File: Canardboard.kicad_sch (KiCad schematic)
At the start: 59 parts, among them J1 RBUS, J4 Conn_01x02_Male, J5 Conn_01x03_Male, J6 Conn_01x03_Male, J7 Conn_01x03_Male, Q1 SI4143DY-T1-GE3, Q2 SI4143DY-T1-GE3, U1 ESP32-S3, U10 LTC4412xS6, U9 LTC4412xS6, Y1 40MHz±10ppm

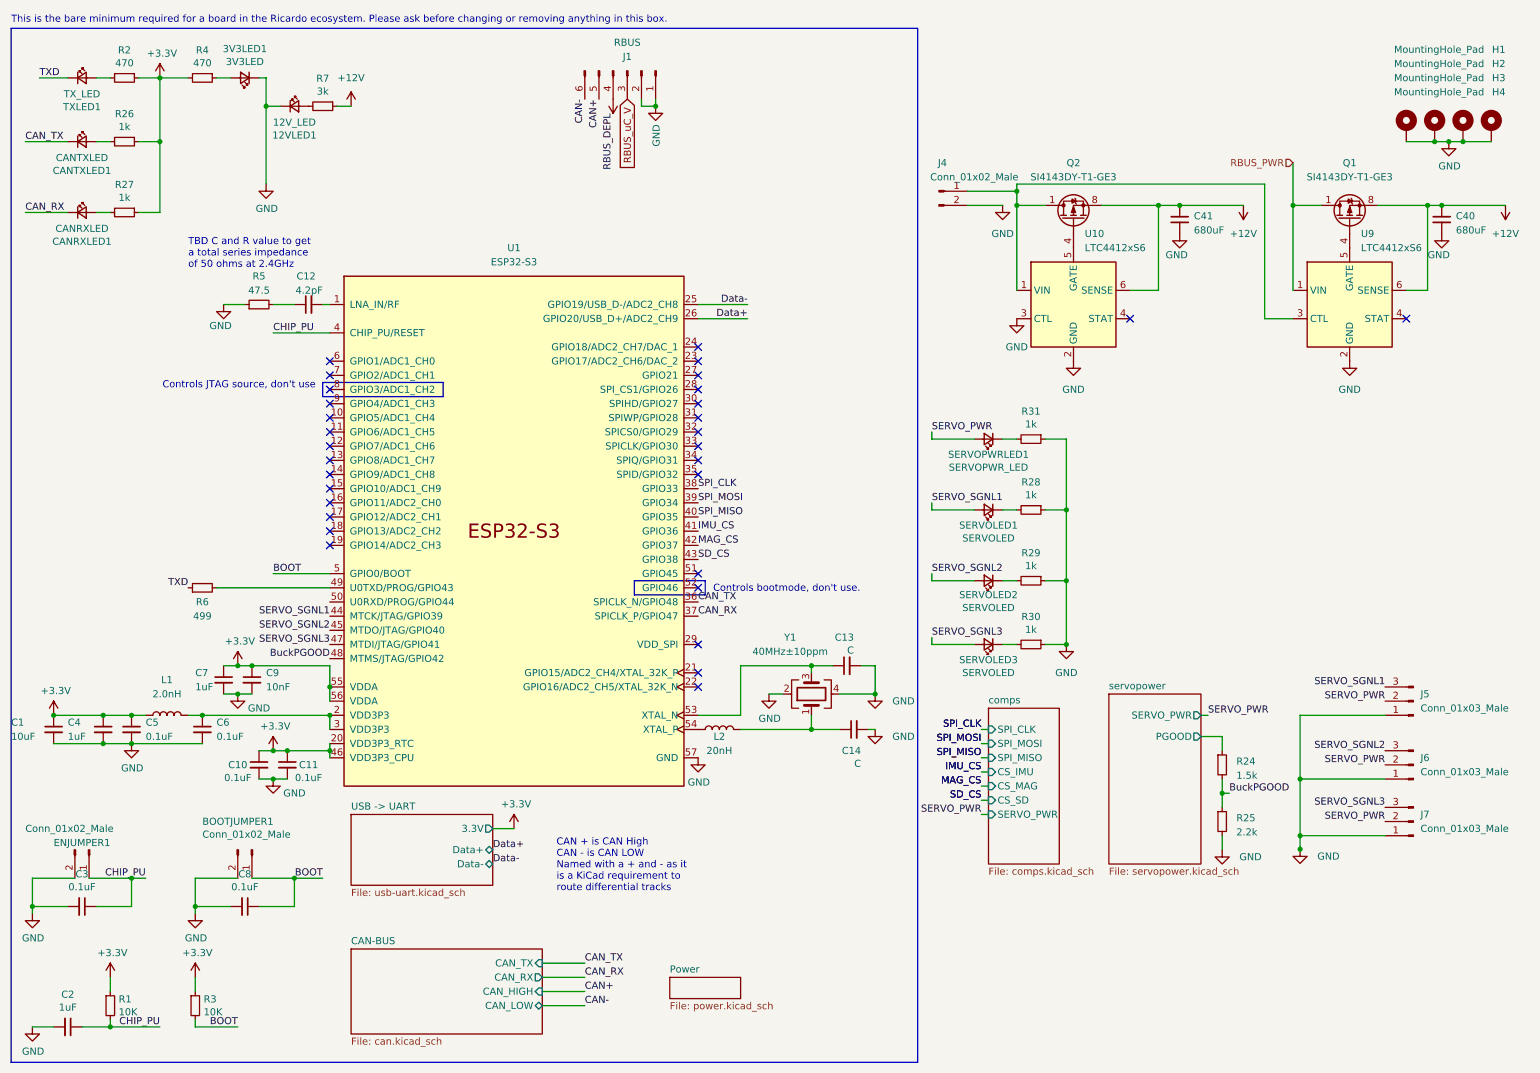
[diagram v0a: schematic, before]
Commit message: error encountered - battery logic and inductor
- use large capacitor?
- use VBUS as a power source?
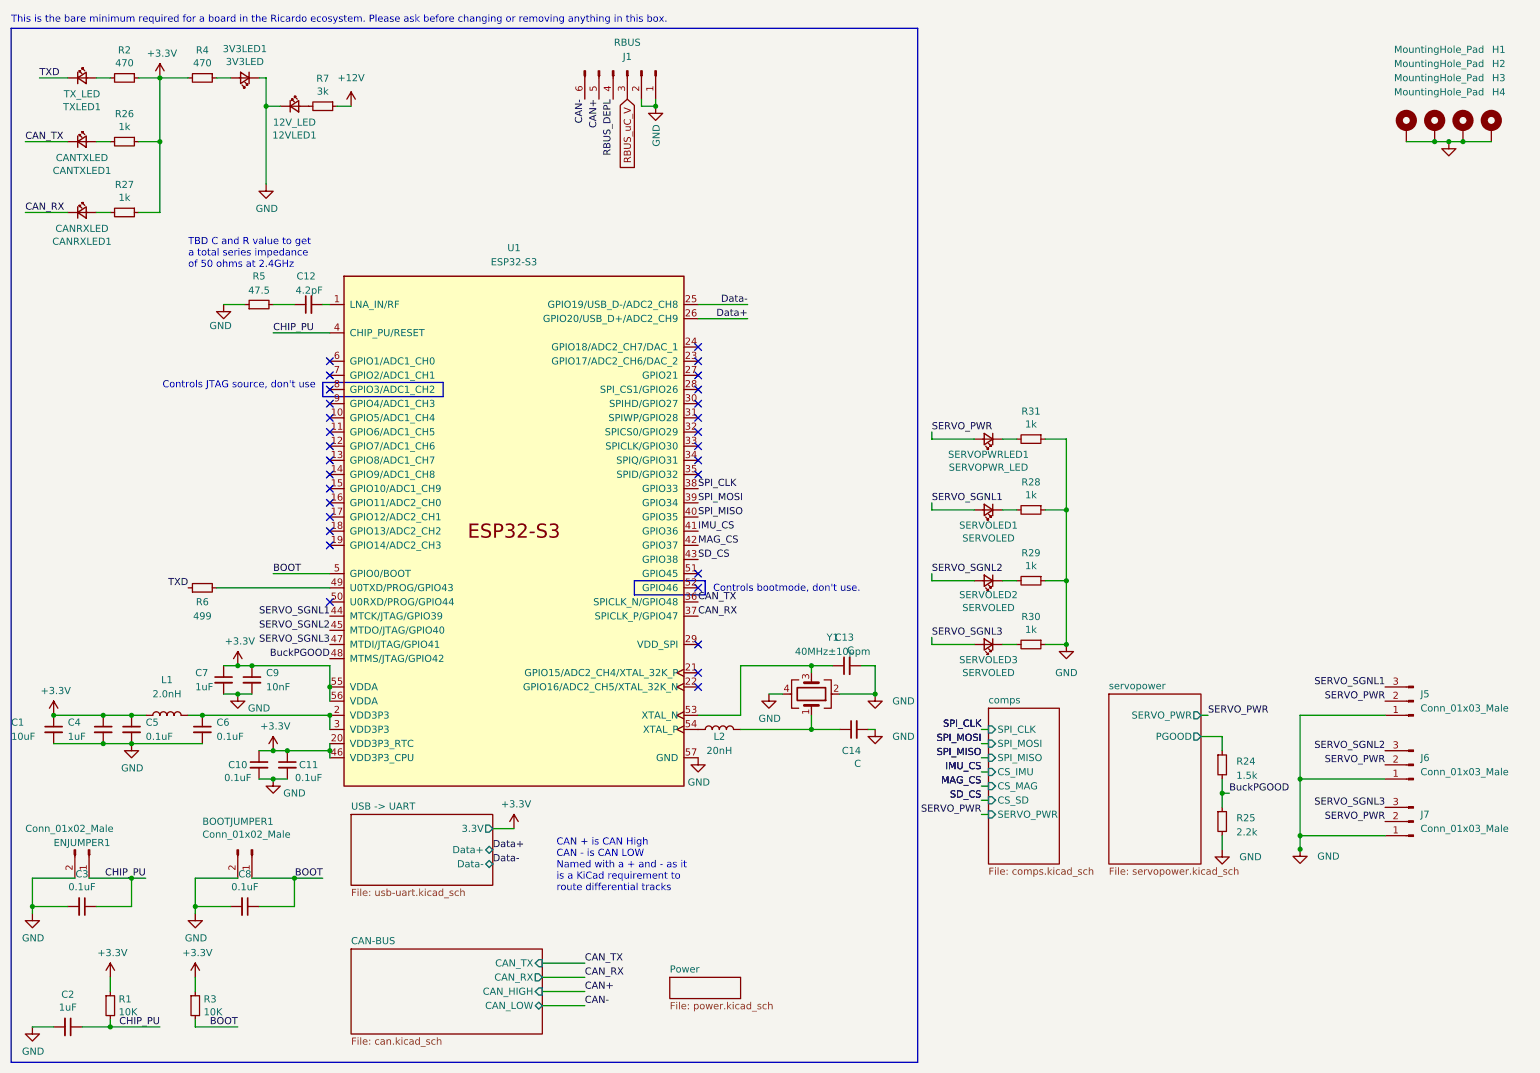
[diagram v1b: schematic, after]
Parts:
- removed C40, C41: 680uF, Capacitor_SMD:CP_Elec_10x10.5, symbol Device:C_Small
- removed J4: Conn_01x02_Male, iclr:AMASS_XT60PW-F, symbol Connector:Conn_01x02_Male
- removed Q1, Q2: SI4143DY-T1-GE3, Package_SO:SOIC-8_3.9x4.9mm_P1.27mm, symbol Device:Q_PMOS_GDS
- removed U10, U9: LTC4412xS6, Package_TO_SOT_SMD:TSOT-23-6, symbol Power_Management:LTC4412xS6
- J1: footprint Connector_Molex:Molex_Mini-Fit_Jr_5566-06A_2x03_P4.20mm_Vertical -> Connector_Molex:Molex_Mini-Fit_Jr_5569-06A2_2x03_P4.20mm_Horizontal
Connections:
- net +12V: no longer J1.4 (Pin_4)
- net RBUS_DEPL: now also J1.4 (Pin_4)
- no-connect marks 31 -> 30
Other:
- moved on the sheet: Y1

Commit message: power draft 2, power fixed I think
10 mosfets now!

2 each on:

Servo power: 3s/4s LIPO, RBUS_DEPL
3.3: VBUS, RBUS_3.3, 3s/4s LIPO

fixed some capacitors
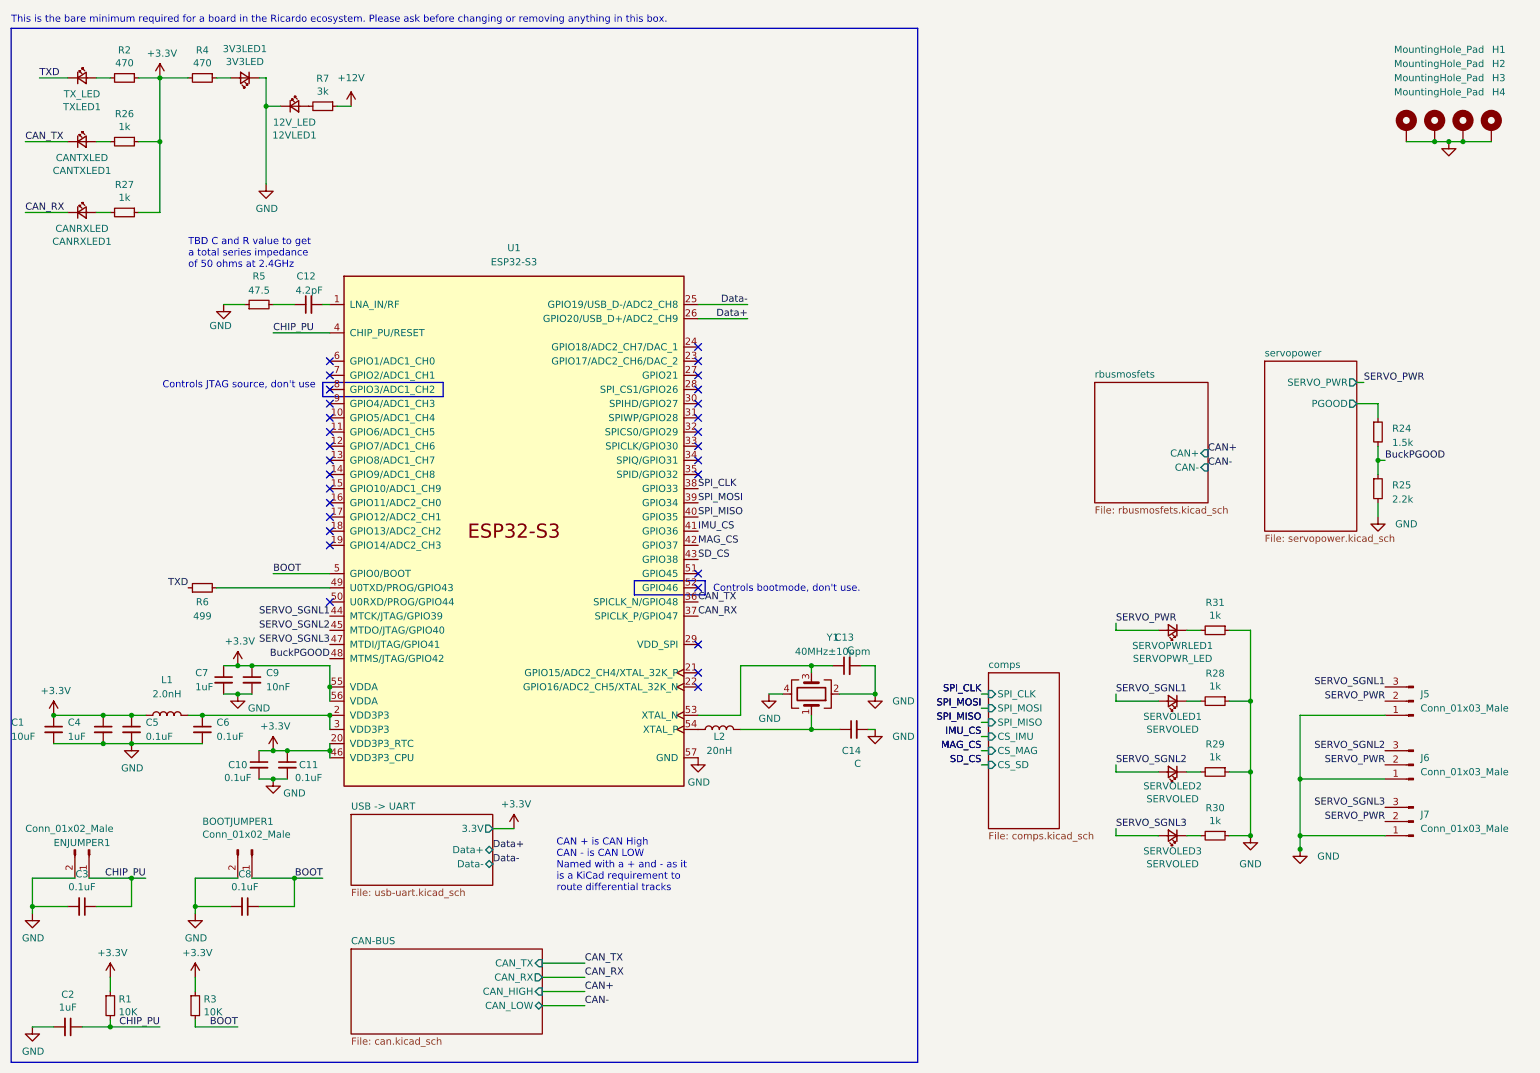
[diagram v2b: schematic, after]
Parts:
- removed J1: RBUS, Connector_Molex:Molex_Mini-Fit_Jr_5569-06A2_2x03_P4.20mm_Horizontal, symbol Connector:Conn_01x06_Male
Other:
- removed sheet Power
- added sheet rbusmosfets (rbusmosfets.kicad_sch)
- sheet comps ports: added none; removed SERVO_PWR
- moved on the sheet: R24, R25, R28, R29, R30, R31, SERVOLED1, SERVOLED2, SERVOLED3, SERVOPWRLED1

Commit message: PCB layout work
pcb layout work
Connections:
- net BOOT: now also BOOTJUMPER1.2 (Pin_2); no longer BOOTJUMPER1.1 (Pin_1)
- net GND: no longer BOOTJUMPER1.2 (Pin_2)
- net IMU_CS: now also U1.45 (MTDO/JTAG/GPIO40); no longer U1.41 (GPIO36)
- net MAG_CS: now also U1.47 (MTDI/JTAG/GPIO41); no longer U1.42 (GPIO37)
- net SD_CS: now also U1.38 (GPIO33); no longer U1.43 (GPIO38)
- net SERVO_SGNL1: now also U1.43 (GPIO38); no longer U1.44 (MTCK/JTAG/GPIO39)
- net SERVO_SGNL2: now also U1.42 (GPIO37); no longer U1.45 (MTDO/JTAG/GPIO40)
- net SERVO_SGNL3: now also U1.44 (MTCK/JTAG/GPIO39); no longer U1.47 (MTDI/JTAG/GPIO41)
- net SPI_CLK: now also U1.39 (GPIO34); no longer U1.38 (GPIO33)
- net SPI_MISO: now also U1.41 (GPIO36); no longer U1.40 (GPIO35)
- net SPI_MOSI: now also U1.40 (GPIO35); no longer U1.39 (GPIO34)
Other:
- moved on the sheet: BOOTJUMPER1
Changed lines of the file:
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@@
-    (stroke (width 0) (type default))
-  )
-  (wire (pts (xy 55.88 165.1) (xy 63.5 165.1))
     (stroke (width 0) (type default))
   )
@@
   )
   (wire (pts (xy 35.56 45.72) (xy 39.37 45.72))
+    (stroke (width 0) (type default))
+  )
+  (wire (pts (xy 58.42 165.1) (xy 63.5 165.1))
     (stroke (width 0) (type default))
   )
@@
     (effects (font (size 1.27 1.27)) (justify right bottom))
   )
+  (label "SD_CS" (at 135.89 95.25 0) (fields_autoplaced)
+    (effects (font (size 1.27 1.27)) (justify left bottom))
+  )
+  (label "SERVO_SGNL2" (at 135.89 105.41 0) (fields_autoplaced)
+    (effects (font (size 1.27 1.27)) (justify left bottom))
+  )
   (label "CAN_RX" (at 15.24 45.72 0) (fields_autoplaced)
     (effects (font (size 1.27 1.27)) (justify left bottom))
@@
     (effects (font (size 1.27 1.27)) (justify left bottom))
   )
-  (label "SPI_CLK" (at 135.89 95.25 0) (fields_autoplaced)
-    (effects (font (size 1.27 1.27)) (justify left bottom))
-  )
-  (label "SERVO_SGNL3" (at 69.85 123.19 180) (fields_autoplaced)
+  (label "SERVO_SGNL3" (at 69.85 118.11 180) (fields_autoplaced)
     (effects (font (size 1.27 1.27)) (justify right bottom))
   )
@@
     (effects (font (size 1.27 1.27)) (justify left bottom))
   )
-  (label "SERVO_SGNL2" (at 69.85 120.65 180) (fields_autoplaced)
-    (effects (font (size 1.27 1.27)) (justify right bottom))
-  )
   (label "SERVO_PWR" (at 255.27 76.2 0) (fields_autoplaced)
     (effects (font (size 1.27 1.27)) (justify left bottom))
@@
     (effects (font (size 1.27 1.27)) (justify right bottom))
   )
+  (label "MAG_CS" (at 69.85 123.19 180) (fields_autoplaced)
+    (effects (font (size 1.27 1.27)) (justify right bottom))
+  )
   (label "BOOT" (at 53.34 191.77 180) (fields_autoplaced)
     (effects (font (size 1.27 1.27)) (justify right bottom))
@@
     (effects (font (size 1.27 1.27)) (justify right bottom))
   )
-  (label "SPI_MOSI" (at 135.89 97.79 0) (fields_autoplaced)
+  (label "SPI_CLK" (at 135.89 97.79 0) (fields_autoplaced)
+    (effects (font (size 1.27 1.27)) (justify left bottom))
+  )
+  (label "SERVO_SGNL1" (at 135.89 107.95 0) (fields_autoplaced)
     (effects (font (size 1.27 1.27)) (justify left bottom))
   )
@@
     (effects (font (size 1.27 1.27)) (justify right bottom))
   )
-  (label "SD_CS" (at 135.89 107.95 0) (fields_autoplaced)
-    (effects (font (size 1.27 1.27)) (justify left bottom))
-  )
   (label "CAN_TX" (at 115.57 180.34 0) (fields_autoplaced)
     (effects (font (size 1.27 1.27)) (justify left bottom))
@@
     (effects (font (size 1.27 1.27)) (justify left bottom))
   )
-  (label "MAG_CS" (at 135.89 105.41 0) (fields_autoplaced)
-    (effects (font (size 1.27 1.27)) (justify left bottom))
-  )
   (label "BOOT" (at 68.58 165.1 180) (fields_autoplaced)
     (effects (font (size 1.27 1.27)) (justify right bottom))
@@
     (effects (font (size 1.27 1.27)) (justify right bottom))
   )
-  (label "SERVO_SGNL1" (at 69.85 118.11 180) (fields_autoplaced)
-    (effects (font (size 1.27 1.27)) (justify right bottom))
+  (label "SPI_MOSI" (at 135.89 100.33 0) (fields_autoplaced)
+    (effects (font (size 1.27 1.27)) (justify left bottom))
   )
   (label "SPI_MISO" (at 186.69 137.16 180) (fields_autoplaced)
@@
     (effects (font (size 1.27 1.27)) (justify right bottom))
   )
-  (label "IMU_CS" (at 135.89 102.87 0) (fields_autoplaced)
-    (effects (font (size 1.27 1.27)) (justify left bottom))
-  )
   (label "SD_CS" (at 186.69 144.78 180) (fields_autoplaced)
     (effects (font (size 1.27 1.27)) (justify right bottom))
@@
     (effects (font (size 1.27 1.27)) (justify right bottom))
   )
+  (label "SPI_MISO" (at 135.89 102.87 0) (fields_autoplaced)
+    (effects (font (size 1.27 1.27)) (justify left bottom))
+  )
   (label "BOOT" (at 59.69 110.49 0) (fields_autoplaced)
     (effects (font (size 1.27 1.27)) (justify left bottom))
@@
     (effects (font (size 1.27 1.27)) (justify right bottom))
   )
+  (label "IMU_CS" (at 69.85 120.65 180) (fields_autoplaced)
+    (effects (font (size 1.27 1.27)) (justify right bottom))
+  )
   (label "SERVO_SGNL2" (at 210.82 144.78 0) (fields_autoplaced)
     (effects (font (size 1.27 1.27)) (justify left bottom))
@@
   )
   (label "BuckPGOOD" (at 259.08 90.17 0) (fields_autoplaced)
-    (effects (font (size 1.27 1.27)) (justify left bottom))
-  )
-  (label "SPI_MISO" (at 135.89 100.33 0) (fields_autoplaced)
     (effects (font (size 1.27 1.27)) (justify left bottom))
   )
@@
     )
   )
-  (symbol (lib_id "Connector:Conn_01x02_Male") (at 55.88 160.02 270) (unit 1)
-    (in_bom yes) (on_board yes) (dnp no)
-    (property "Reference" "BOOTJUMPER1" (at 46.99 154.94 90)
+  (symbol (lib_id "Connector:Conn_01x02_Male") (at 55.88 160.02 90) (mirror x) (unit 1)
+    (in_bom yes) (on_board yes) (dnp no)
+    (property "Reference" "BOOTJUMPER1" (at 64.77 154.94 90)
       (effects (font (size 1.27 1.27)) (justify left))
     )
-    (property "Value" "Conn_01x02_Male" (at 46.99 157.2514 90)
+    (property "Value" "Conn_01x02_Male" (at 64.77 157.2514 90)
       (effects (font (size 1.27 1.27)) (justify left))
     )
